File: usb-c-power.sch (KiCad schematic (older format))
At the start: 22 parts

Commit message: update dcdc feedback config & components
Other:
- note removed: "TODO: Add cap on output ?"
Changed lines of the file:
@@
 $EndComp
 NoConn ~ 5350 4100
-Text Notes 2400 2500 0    50   ~ 0
-TODO: Add cap on output ?
 Wire Wire Line
 	8650 3150 8650 3550

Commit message: switch components supplier to Mouser for price/availability
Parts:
- J?: Supplier Digi-Key -> Mouser; Supplier Part Number 12401610E4#2ACT-ND -> 523-12401610E4#2A
- Q?: Supplier Digi-Key -> Mouser; Supplier Part Number NTR2101PT1GOSCT-ND -> 863-NTR2101PT1G
- U?: Supplier Digi-Key -> Mouser; Supplier Part Number UTC2000-I/MG-ND -> 579-UTC2000-I/MG
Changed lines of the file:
@@
 F 5 "Microchip Technology" H 6250 3250 60  0001 C CNN "Manufacturer"
 F 6 "UTC2000-I/MG" H 6250 3250 60  0001 C CNN "Manufacturer Part Number"
-F 7 "Digi-Key" H 6250 3250 60  0001 C CNN "Supplier"
-F 8 "UTC2000-I/MG-ND" H 6250 3250 60  0001 C CNN "Supplier Part Number"
+F 7 "Mouser" H 6250 3250 60  0001 C CNN "Supplier"
+F 8 "579-UTC2000-I/MG" H 6250 3250 60  0001 C CNN "Supplier Part Number"
 	1    6250 4000
 	1    0    0    -1
@@
 F 5 "ON Semiconductor" H 8650 2950 50  0001 L CNN "Manufacturer"
 F 6 "NTR2101PT1G" H 8650 2950 50  0001 L CNN "Manufacturer Part Number"
-F 7 "Digi-Key" H 8650 2950 50  0001 L CNN "Supplier"
-F 8 "NTR2101PT1GOSCT-ND" H 8650 2950 50  0001 L CNN "Supplier Part Number"
+F 7 "Mouser" H 8650 2950 50  0001 L CNN "Supplier"
+F 8 "863-NTR2101PT1G" H 8650 2950 50  0001 L CNN "Supplier Part Number"
 	1    8650 2950
 	0    1    -1   0
@@
 F 5 "Amphenol ICC (Commercial Products)" H -150 -50 50  0001 C CNN "Manufacturer"
 F 6 "12401610E4#2A" H -150 -50 50  0001 C CNN "Manufacturer Part Number"
-F 7 "Digi-Key" H -150 -50 50  0001 C CNN "Supplier"
-F 8 "12401610E4#2ACT-ND" H -150 -50 50  0001 C CNN "Supplier Part Number"
+F 7 "Mouser" H -150 -50 50  0001 C CNN "Supplier"
+F 8 "523-12401610E4#2A" H -150 -50 50  0001 C CNN "Supplier Part Number"
 	1    2700 3850
 	1    0    0    -1

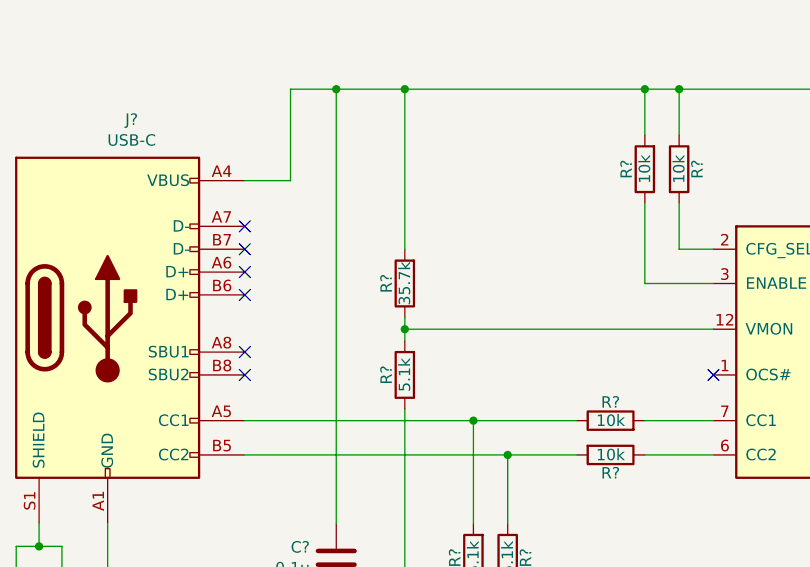
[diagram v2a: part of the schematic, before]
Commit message: fix audio pot label & other label sizing
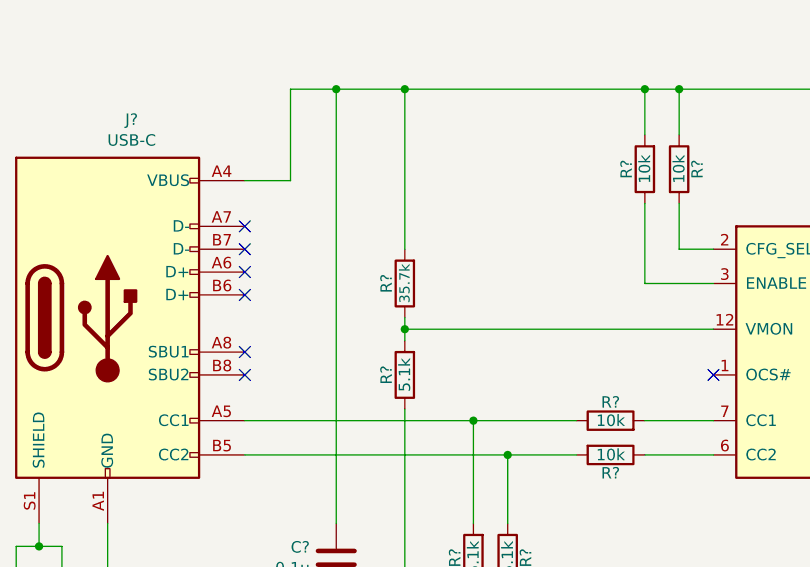
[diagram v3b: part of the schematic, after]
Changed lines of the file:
@@
 P 4000 3700
 F 0 "R?" V 4080 3700 50  0000 C CNN
-F 1 "35.7k" V 4000 3700 50  0000 C CNN
+F 1 "35.7k" V 4000 3700 45  0000 C CNN
 F 2 "Resistor_SMD:R_0805_2012Metric_Pad1.15x1.40mm_HandSolder" V 3930 3700 50  0001 C CNN
 F 3 "https://industrial.panasonic.com/cdbs/www-data/pdf/RDA0000/AOA0000C304.pdf" H 4000 3700 50  0001 C CNN

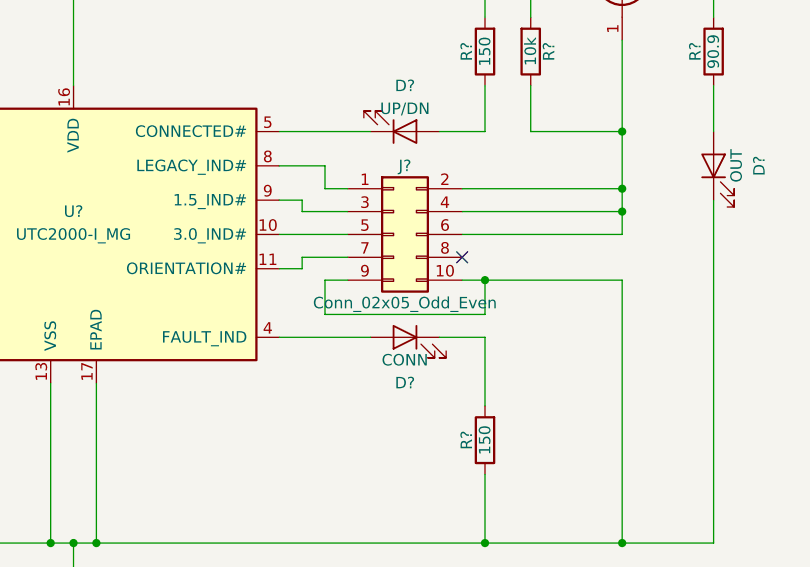
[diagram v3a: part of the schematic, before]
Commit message: update usb indicators breakout
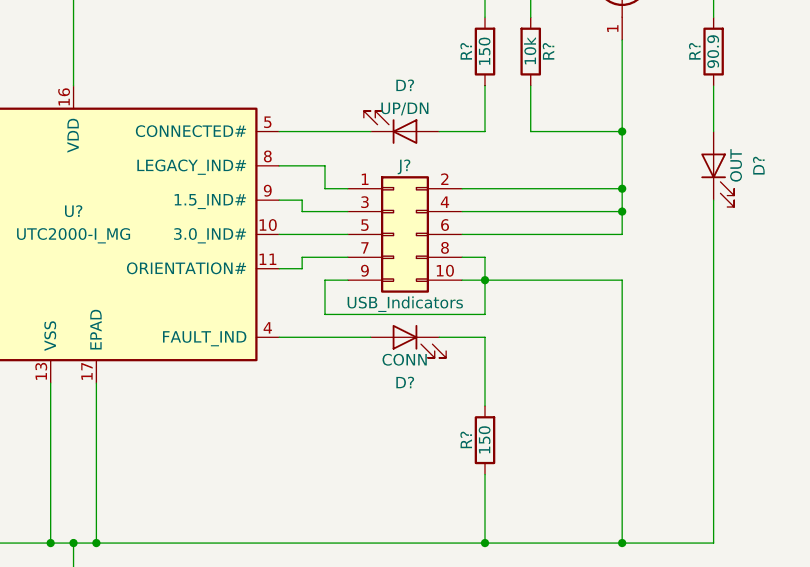
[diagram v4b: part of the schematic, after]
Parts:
- J?: value Conn_02x05_Odd_Even -> USB_Indicators
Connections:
- net GND: now also J?.8 (Pin_8)
- no-connect marks 8 -> 7
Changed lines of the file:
@@
 P 7650 4000
 F 0 "J?" H 7700 4300 50  0000 C CNN
-F 1 "Conn_02x05_Odd_Even" H 7700 3700 50  0000 C CNN
+F 1 "USB_Indicators" H 7700 3700 50  0000 C CNN
 F 2 "Connector_PinHeader_2.54mm:PinHeader_2x05_P2.54mm_Vertical" H 7650 4000 50  0001 C CNN
 F 3 "https://drawings-pdf.s3.amazonaws.com/11636.pdf" H 7650 4000 50  0001 C CNN
@@
 Wire Wire Line
 	8050 4200 8650 4200
-NoConn ~ 7950 4100
 $Comp
 L Device:R R?
@@
 	3500 2850 3700 2850
 Connection ~ 3700 2850
+Wire Wire Line
+	7950 4100 8050 4100
+Wire Wire Line
+	8050 4100 8050 4200
 $EndSCHEMATC
